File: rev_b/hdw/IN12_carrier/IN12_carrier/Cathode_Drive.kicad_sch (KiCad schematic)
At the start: 22 parts, among them Q901 MMSTA42, Q902 MMSTA42, Q904 MMSTA42, Q905 MMSTA42, Q906 MMSTA42, Q907 MMSTA42, Q908 MMSTA42, Q909 MMSTA42, Q910 MMSTA42, Q911 MMSTA42

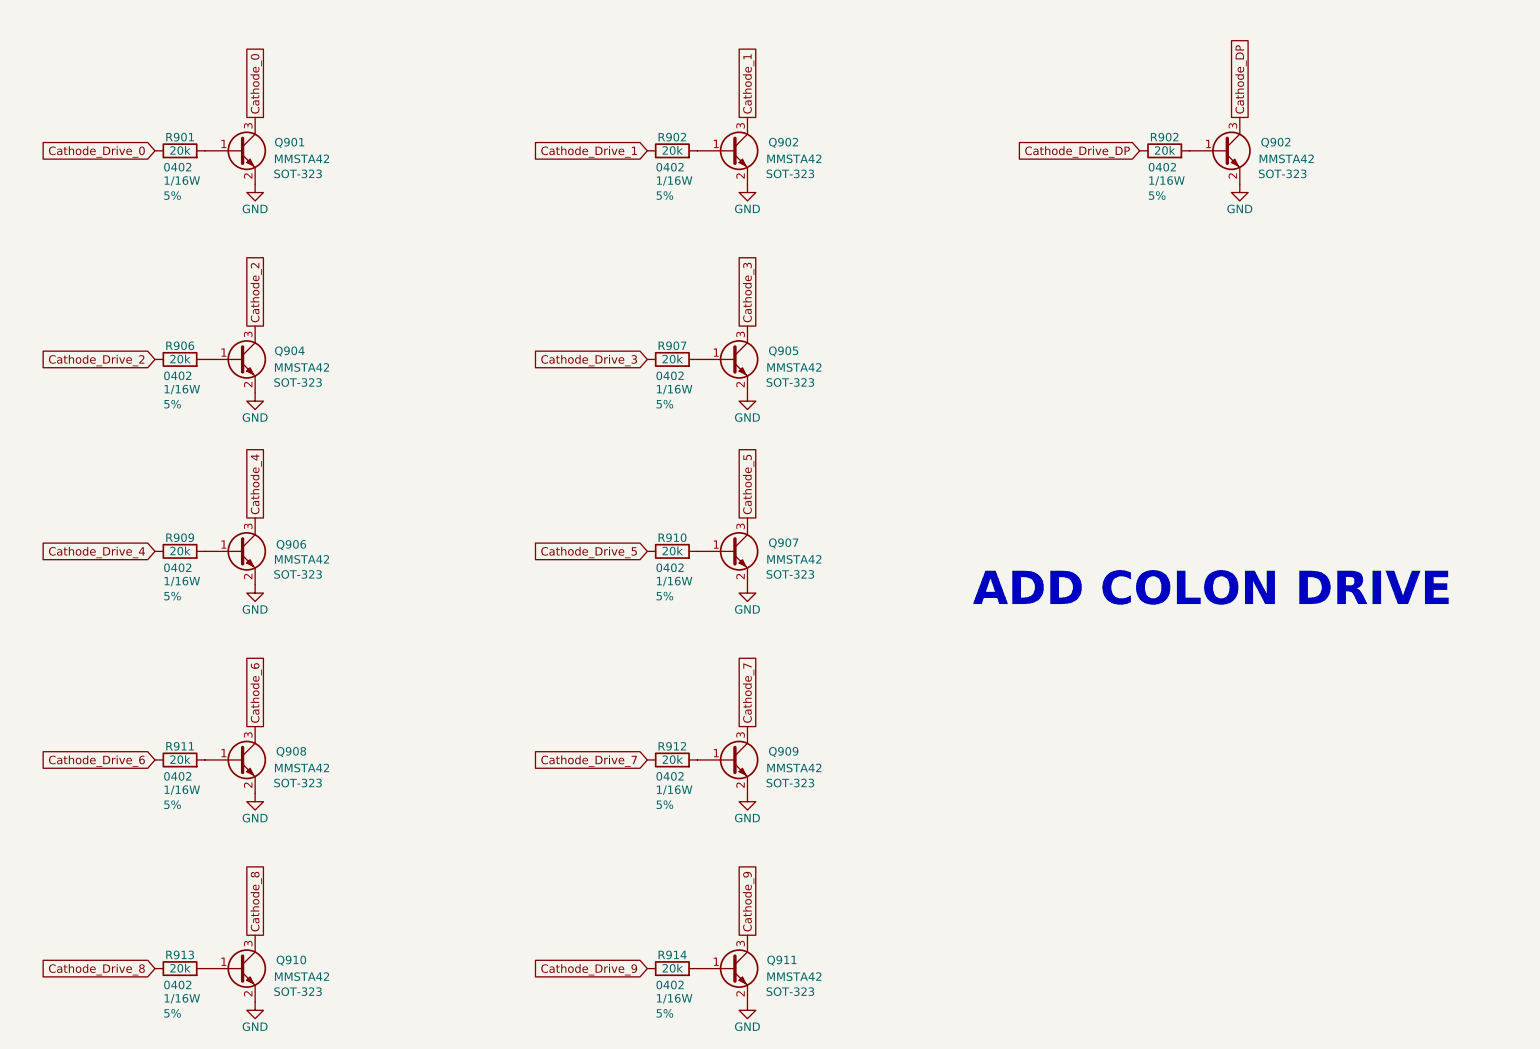
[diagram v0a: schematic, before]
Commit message: updated footprints, ran some DRC
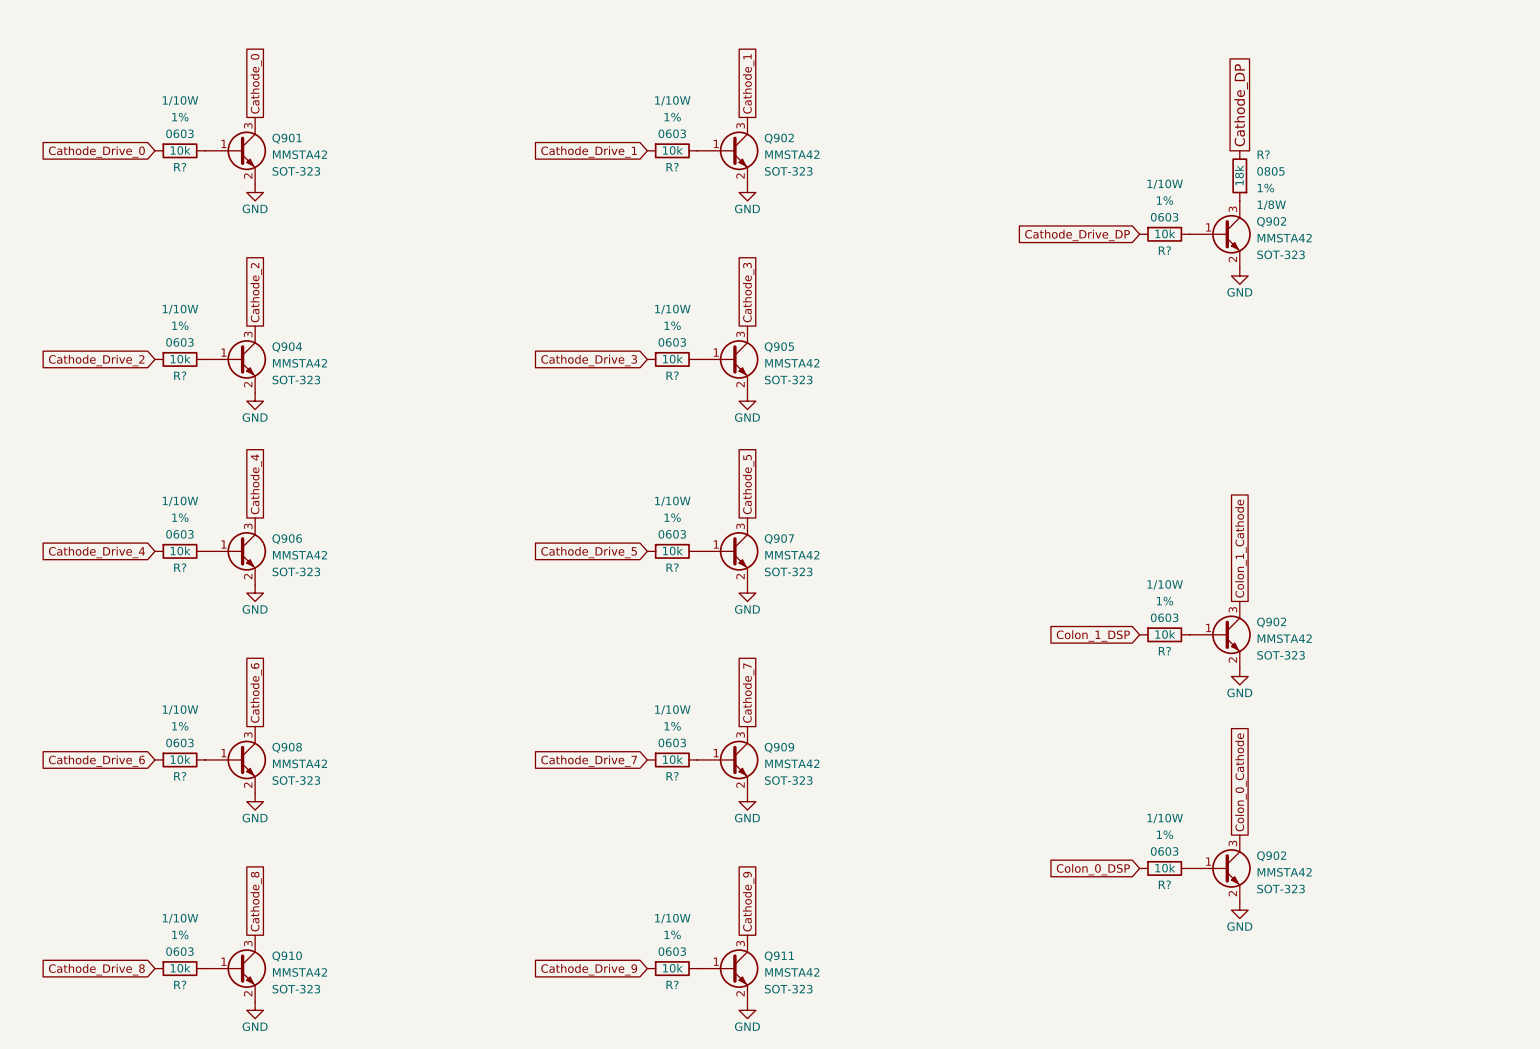
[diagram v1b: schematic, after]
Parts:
- removed R901, R902 (x2), R906, R907, R909, R910, R911, R912, R913, R914: 20k, Resistors_SMD:R_0402, symbol Nixie-Clock-rescue:R
- added Q902 (x2): MMSTA42, TO_SOT_Packages_SMD:SOT-323_SC-70, symbol Nixie-Clock-rescue:Q_NPN_BEC
- added R? (x13): 10k, Resistors_SMD:R_0603, symbol Custom Library:R_Custom
- added R?: 18k, Resistors_SMD:R_0805, symbol Custom Library:R_Custom
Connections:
- net Cathode_DP: now also R?.2; no longer Q902.3 (C)
- net Cathode_Drive_0: now also R?.1
- net Cathode_Drive_1: now also R?.1
- net Cathode_Drive_2: now also R?.1
- net Cathode_Drive_3: now also R?.1
- net Cathode_Drive_4: now also R?.1
- net Cathode_Drive_5: now also R?.1
- net Cathode_Drive_6: now also R?.1
- net Cathode_Drive_7: now also R?.1
- net Cathode_Drive_8: now also R?.1
- net Cathode_Drive_9: now also R?.1
- net Cathode_Drive_DP: now also R?.1
- net GND: now also Q902.2 (E), Q902.2 (E)
- net at Q902.1 (B): now also R?.2 (x2)
- net at Q910.1 (B): now also R?.2
- net at Q904.1 (B): now also R?.2
- net at Q909.1 (B): now also R?.2
- net at Q901.1 (B): now also R?.2
- net at Q907.1 (B): now also R?.2
- net at Q911.1 (B): now also R?.2
- net at Q908.1 (B): now also R?.2
- net at Q906.1 (B): now also R?.2
- net at Q905.1 (B): now also R?.2
- new net: Q902.1 (B), R?.2 (x2)
- new net: Q902.3 (C), R?.1
- new net Colon_0_Cathode: Q902.3 (C)
- new net Colon_0_DSP: R?.1
- new net Colon_1_Cathode: Q902.3 (C)
- new net Colon_1_DSP: R?.1
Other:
- note removed: "ADD COLON DRIVE"
- moved on the sheet: Q902

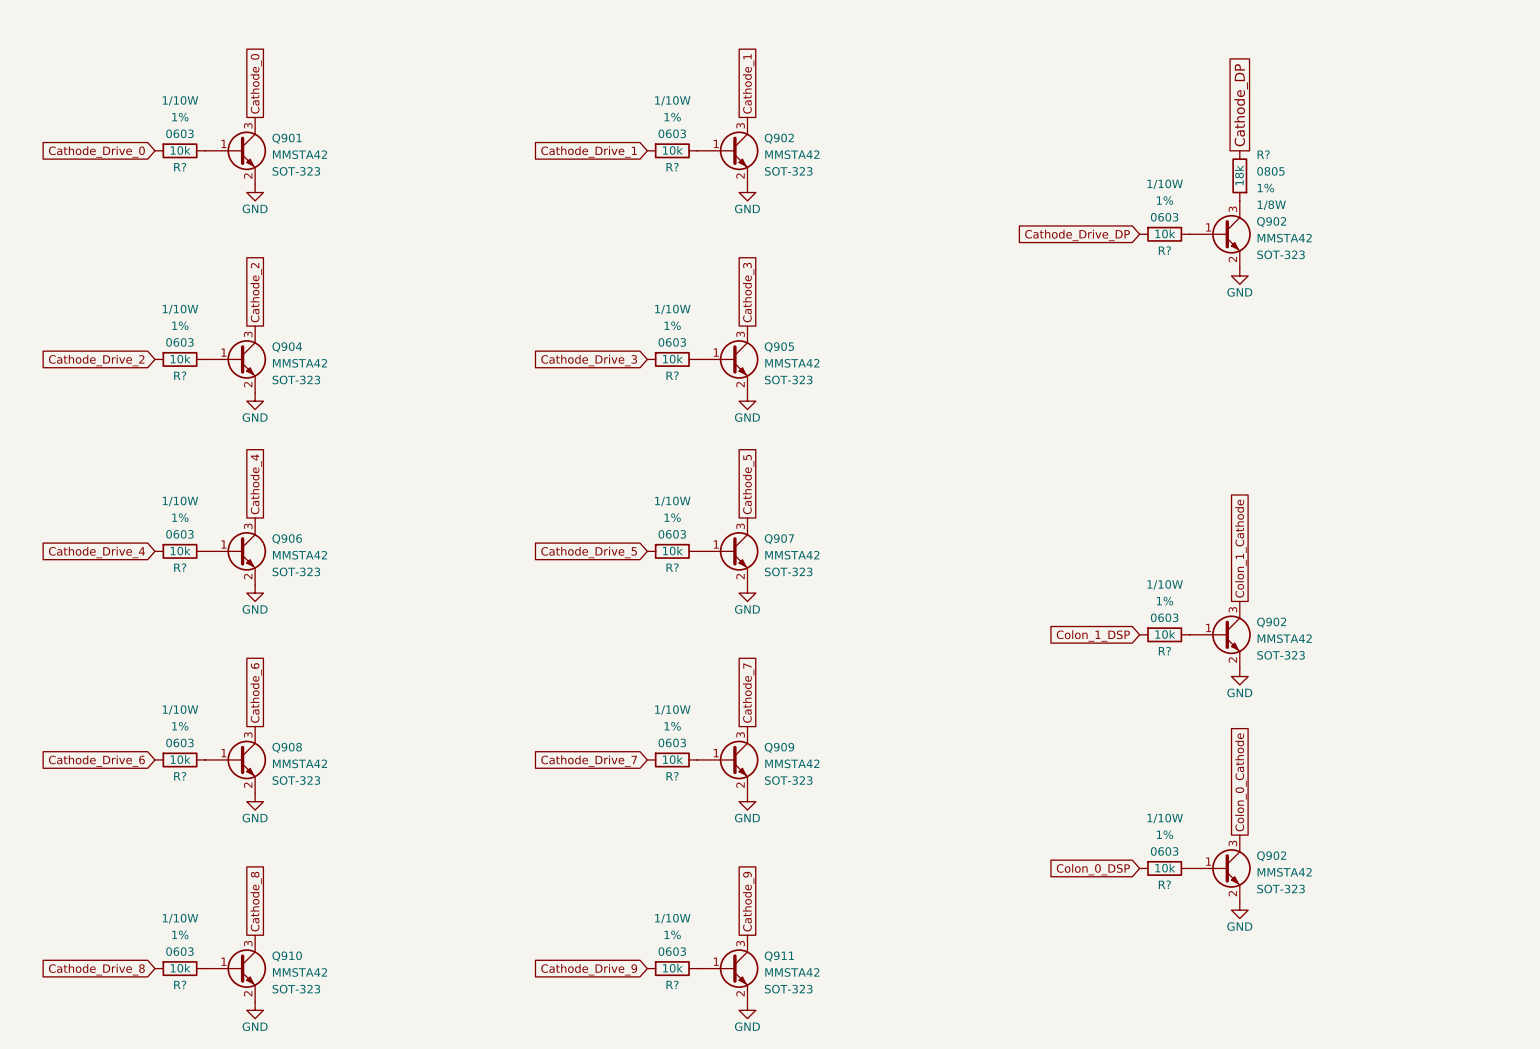
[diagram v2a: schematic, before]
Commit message: lots of placement progress on IN12 carrier board
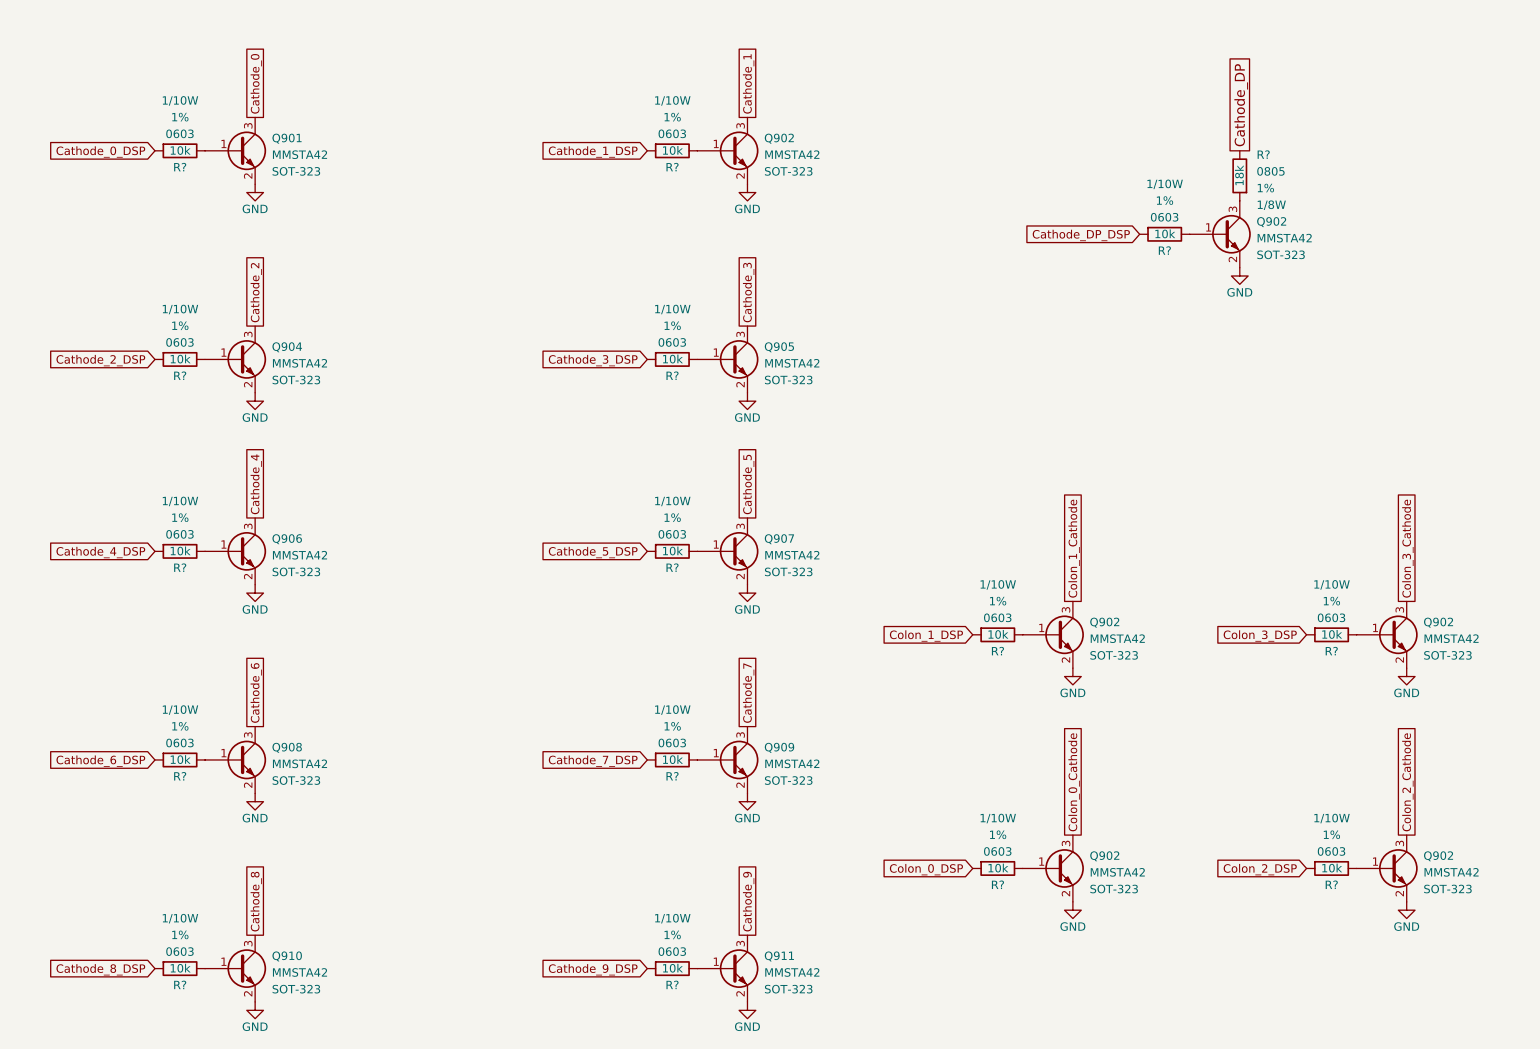
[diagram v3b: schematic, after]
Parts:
- added Q902 (x2): MMSTA42, TO_SOT_Packages_SMD:SOT-323_SC-70, symbol Nixie-Clock-rescue:Q_NPN_BEC
- added R? (x2): 10k, Resistors_SMD:R_0603, symbol Custom Library:R_Custom
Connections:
- net GND: now also Q902.2 (E), Q902.2 (E)
- net Cathode_Drive_0 renamed Cathode_0_DSP
- net Cathode_Drive_1 renamed Cathode_1_DSP
- net Cathode_Drive_2 renamed Cathode_2_DSP
- net Cathode_Drive_3 renamed Cathode_3_DSP
- net Cathode_Drive_4 renamed Cathode_4_DSP
- net Cathode_Drive_5 renamed Cathode_5_DSP
- net Cathode_Drive_6 renamed Cathode_6_DSP
- net Cathode_Drive_7 renamed Cathode_7_DSP
- net Cathode_Drive_8 renamed Cathode_8_DSP
- net Cathode_Drive_9 renamed Cathode_9_DSP
- net Cathode_Drive_DP renamed Cathode_DP_DSP
- new net: Q902.1 (B), R?.2 (x2)
- new net Colon_2_Cathode: Q902.3 (C)
- new net Colon_2_DSP: R?.1
- new net Colon_3_Cathode: Q902.3 (C)
- new net Colon_3_DSP: R?.1
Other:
- moved on the sheet: Q902, R?
